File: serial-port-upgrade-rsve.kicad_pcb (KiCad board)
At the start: 4 copper layers, 35.6 x 43.2 mm, 14 parts, among them J1 MFP RC, J2 MFP TDO, J3 VCC, J4 GND, J5 Led, J6 IDC connector, U1 GAL16V8_PHY, U2 12-STAGE_BINARY_RIPPLE_COUNTE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, X1 1,8432 MHz

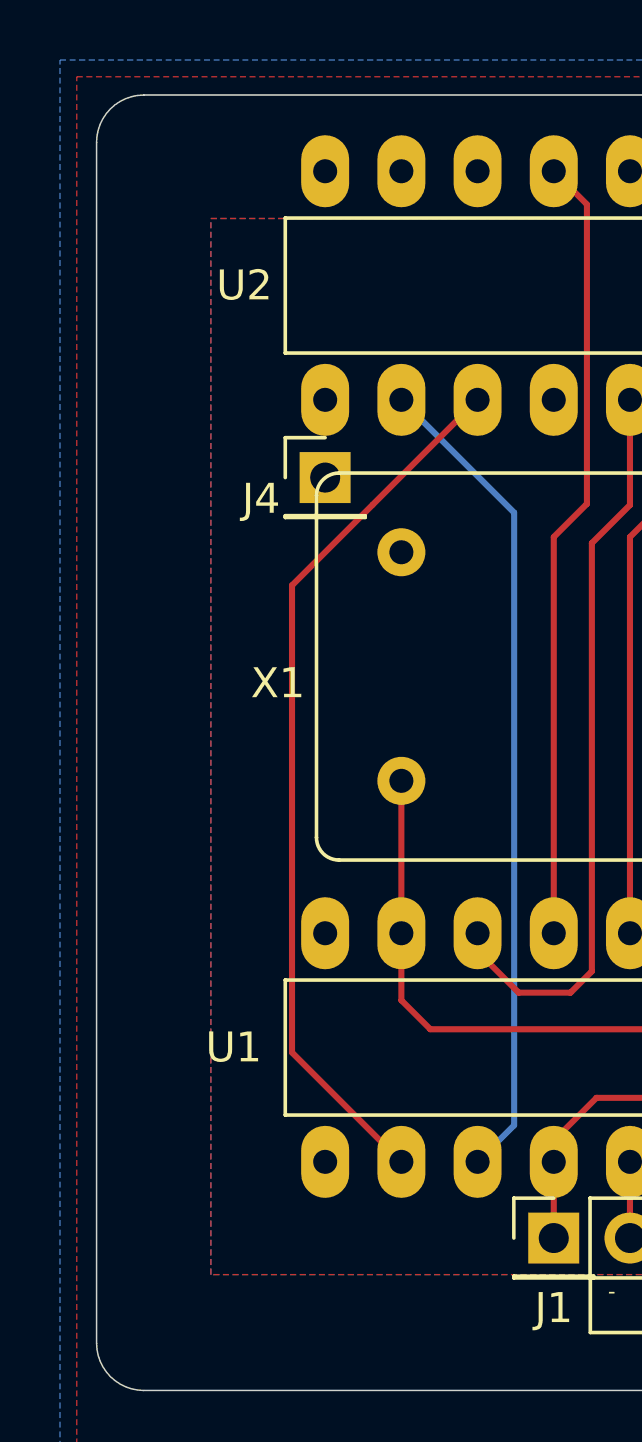
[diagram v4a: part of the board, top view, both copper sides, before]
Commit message: licence logo, title and disclaimer on PCB
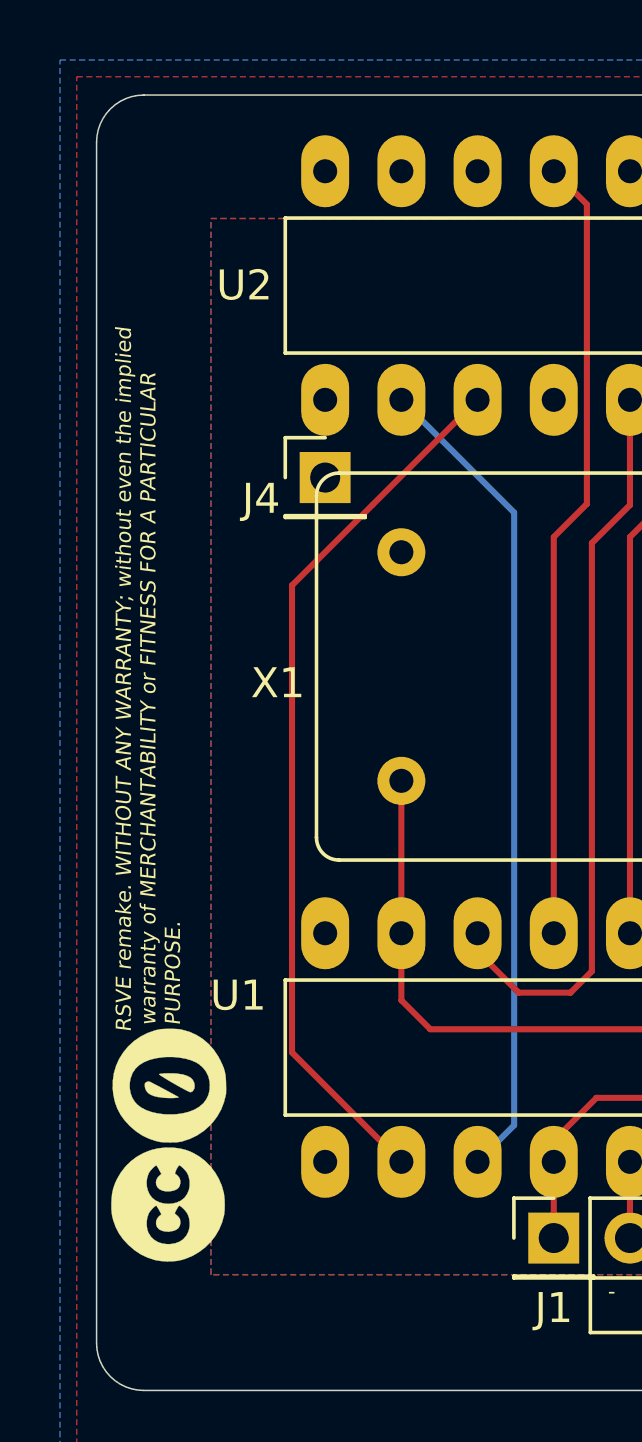
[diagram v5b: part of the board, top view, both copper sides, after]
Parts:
- added G***: LOGO, cliparts:logo--cc--zero, F.Cu at (78.6, 109.2)
- added G***: LOGO, cliparts:logo--cc--cc, F.Cu at (78.6, 113.1)
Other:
- board text added: "RSVE remake. WITHOUT ANY WARRANTY; without even the implied warranty of MERCHANTABILITY or FITNESS FOR A PARTICULAR PURPOSE."

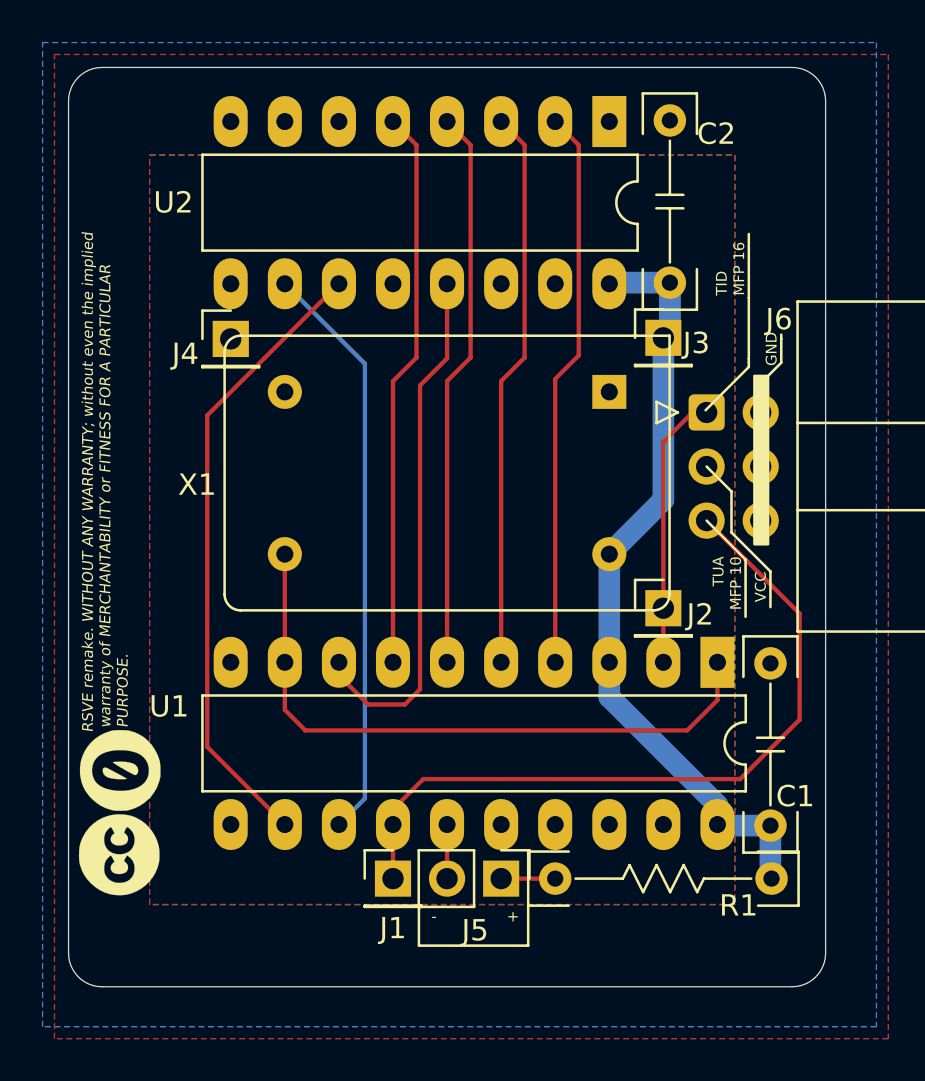
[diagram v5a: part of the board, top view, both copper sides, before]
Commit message: added mounting hole
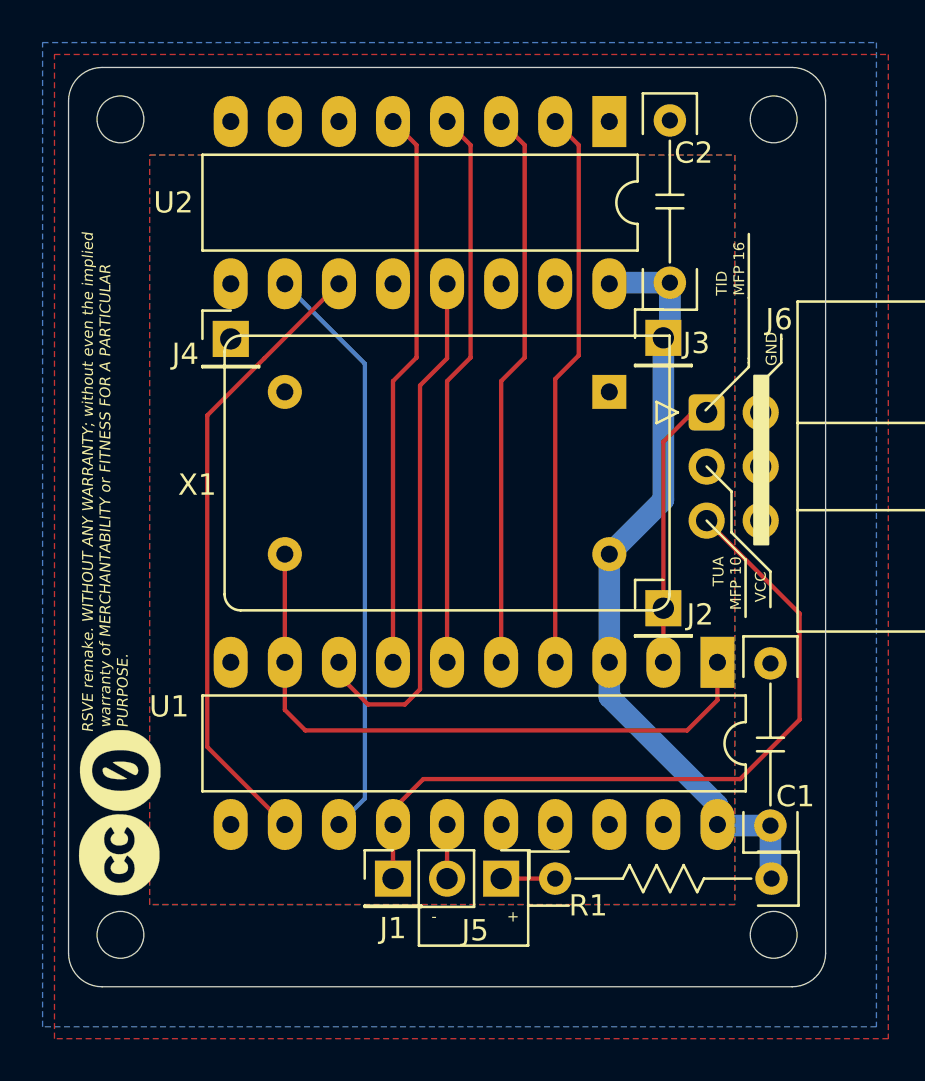
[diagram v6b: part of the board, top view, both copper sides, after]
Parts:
- added H1: M2, MountingHole:MountingHole_2.2mm_M2, F.Cu at (78.6, 78.6)
- added H2: M2, MountingHole:MountingHole_2.2mm_M2, F.Cu at (109.3, 78.6)
- added H3: M2, MountingHole:MountingHole_2.2mm_M2, F.Cu at (109.3, 116.9)
- added H4: M2, MountingHole:MountingHole_2.2mm_M2, F.Cu at (78.6, 116.9)
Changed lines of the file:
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@@
     (tracks 63)
     (zones 0)
-    (modules 16)
+    (modules 20)
     (nets 27)
   )
@@
     (add_net GND)
     (add_net VCC)
+  )
+  (module MountingHole:MountingHole_2.2mm_M2 (layer F.Cu)
+    (at 78.6384 116.8908)
+    (descr "Mounting Hole 2.2mm, no annular, M2")
+    (tags "mounting hole 2.2mm no annular m2")
+    (attr virtual)
+    (fp_text reference H4 (at 0 -3.2) (layer F.Fab)
+      (effects (font (size 1 1) (thickness 0.15)))
+    )
+    (fp_text value M2 (at 0 3.2) (layer F.Fab)
+      (effects (font (size 1 1) (thickness 0.15)))
+    )
+    (fp_text user %R (at 0.3 0) (layer F.Fab)
+      (effects (font (size 1 1) (thickness 0.15)))
+    )
+    (fp_circle (center 0 0) (end 2.2 0) (layer Cmts.User) (width 0.15))
+    (fp_circle (center 0 0) (end 2.45 0) (layer F.CrtYd) (width 0.05))
+    (pad 1 np_thru_hole circle (at 0 0) (size 2.2 2.2) (drill 2.2) (layers *.Cu *.Mask))
+  )
+  (module MountingHole:MountingHole_2.2mm_M2 (layer F.Cu)
+    (at 109.3216 116.8908)
+    (descr "Mounting Hole 2.2mm, no annular, M2")
+    (tags "mounting hole 2.2mm no annular m2")
+    (attr virtual)
+    (fp_text reference H3 (at 0 -3.2) (layer F.Fab)
+      (effects (font (size 1 1) (thickness 0.15)))
+    )
+    (fp_text value M2 (at 0 3.2) (layer F.Fab)
+      (effects (font (size 1 1) (thickness 0.15)))
+    )
+    (fp_text user %R (at 0.3 0) (layer F.Fab)
+      (effects (font (size 1 1) (thickness 0.15)))
+    )
+    (fp_circle (center 0 0) (end 2.2 0) (layer Cmts.User) (width 0.15))
+    (fp_circle (center 0 0) (end 2.45 0) (layer F.CrtYd) (width 0.05))
+    (pad 1 np_thru_hole circle (at 0 0) (size 2.2 2.2) (drill 2.2) (layers *.Cu *.Mask))
+  )
+  (module MountingHole:MountingHole_2.2mm_M2 (layer F.Cu)
+    (at 109.3216 78.5876)
+    (descr "Mounting Hole 2.2mm, no annular, M2")
+    (tags "mounting hole 2.2mm no annular m2")
+    (attr virtual)
+    (fp_text reference H2 (at 0 -3.2) (layer F.Fab)
+      (effects (font (size 1 1) (thickness 0.15)))
+    )
+    (fp_text value M2 (at 0 3.2) (layer F.Fab)
+      (effects (font (size 1 1) (thickness 0.15)))
+    )
+    (fp_text user %R (at 0.3 0) (layer F.Fab)
+      (effects (font (size 1 1) (thickness 0.15)))
+    )
+    (fp_circle (center 0 0) (end 2.2 0) (layer Cmts.User) (width 0.15))
+    (fp_circle (center 0 0) (end 2.45 0) (layer F.CrtYd) (width 0.05))
+    (pad 1 np_thru_hole circle (at 0 0) (size 2.2 2.2) (drill 2.2) (layers *.Cu *.Mask))
+  )
+  (module MountingHole:MountingHole_2.2mm_M2 (layer F.Cu)
+    (at 78.6384 78.5876)
+    (descr "Mounting Hole 2.2mm, no annular, M2")
+    (tags "mounting hole 2.2mm no annular m2")
+    (attr virtual)
+    (fp_text reference H1 (at 0 -3.2) (layer F.Fab)
+      (effects (font (size 1 1) (thickness 0.15)))
+    )
+    (fp_text value M2 (at 0 3.2) (layer F.Fab)
+      (effects (font (size 1 1) (thickness 0.15)))
+    )
+    (fp_text user %R (at 0.3 0) (layer F.Fab)
+      (effects (font (size 1 1) (thickness 0.15)))
+    )
+    (fp_circle (center 0 0) (end 2.2 0) (layer Cmts.User) (width 0.15))
+    (fp_circle (center 0 0) (end 2.45 0) (layer F.CrtYd) (width 0.05))
+    (pad 1 np_thru_hole circle (at 0 0) (size 2.2 2.2) (drill 2.2) (layers *.Cu *.Mask))
   )
   (module cliparts:logo--cc--zero (layer F.Cu)
@@
     (descr "THT resistor, width 100mils, lead vias 400mils apart")
     (tags "axial resistor tht")
-    (fp_text reference R1 (at -4.445 -1.27) (layer F.SilkS)
-      (effects (font (size 1 1) (thickness 0.15)) (justify right))
+    (fp_text reference R1 (at 4.445 -1.27) (layer F.SilkS)
+      (effects (font (size 1 1) (thickness 0.15)) (justify left))
     )
     (fp_text value 1K (at 0 -0.5) (layer F.Fab)
@@
     (descr "MLCC THT axial capacitor, width 100mils, lead vias 300mils apart")
     (tags "mlcc axial capacitor tht")
-    (fp_text reference C2 (at 3.175 1.27 180) (layer F.SilkS)
+    (fp_text reference C2 (at 2.286 0.2032 180) (layer F.SilkS)
       (effects (font (size 1 1) (thickness 0.15)) (justify left))
     )

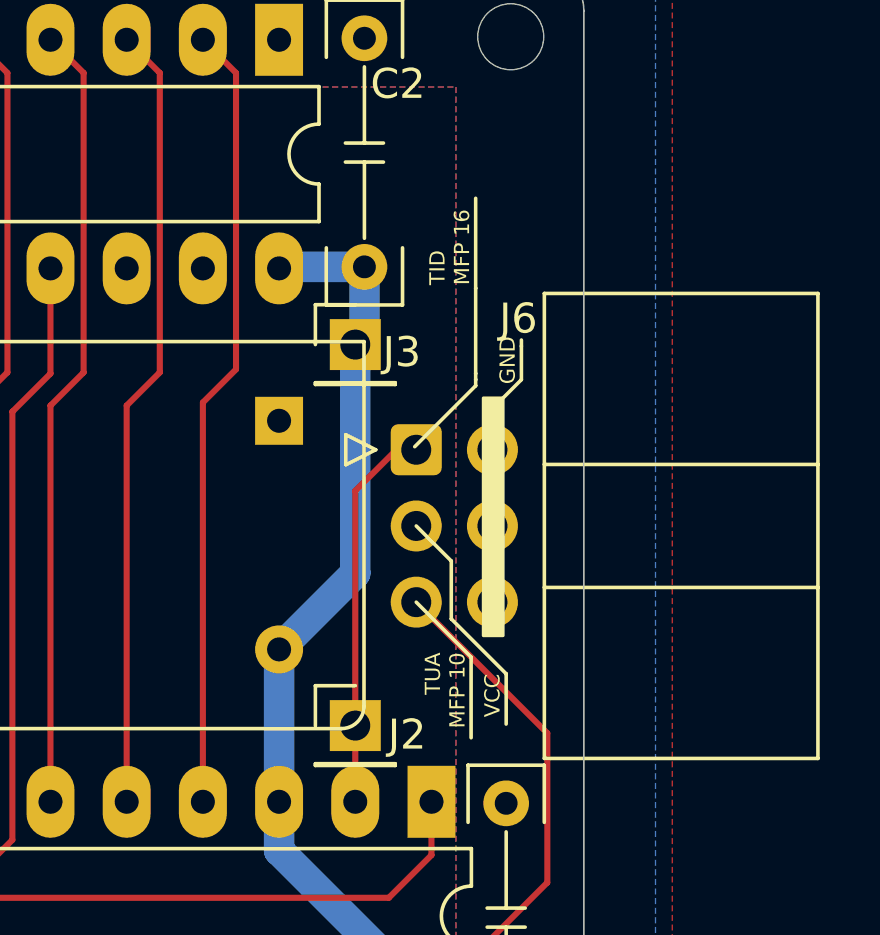
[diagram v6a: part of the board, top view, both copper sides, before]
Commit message: silkscreen : replace MFP pin number mentions (DIP 48 specific) by pin names
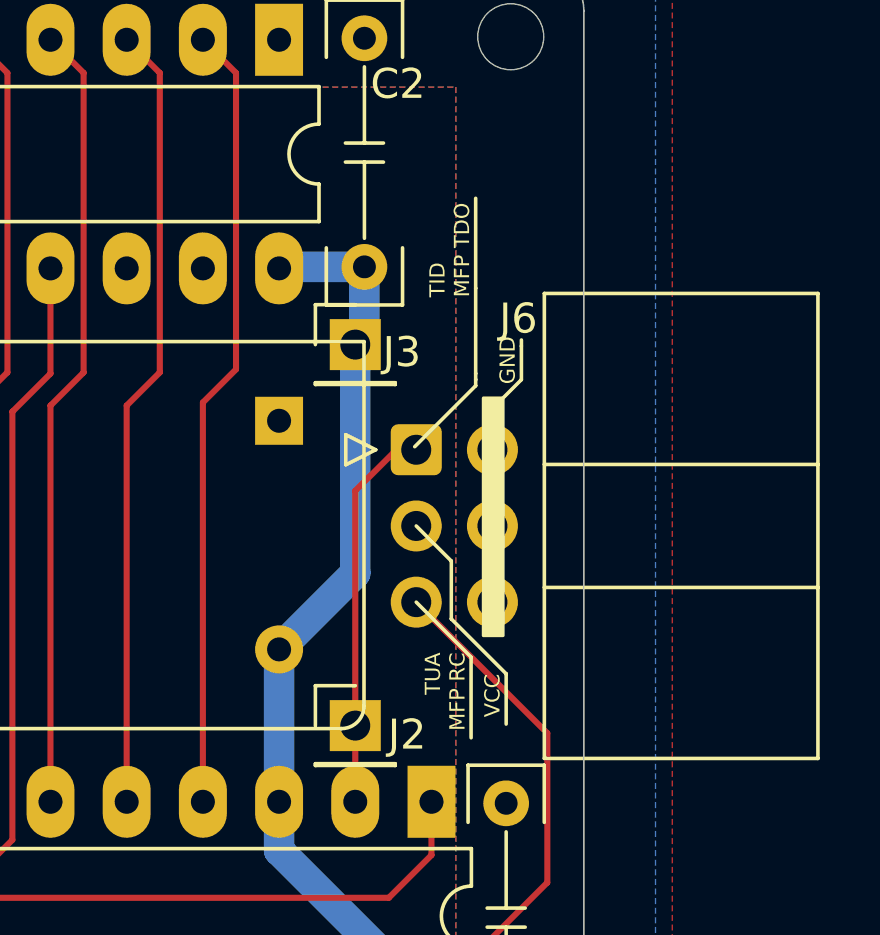
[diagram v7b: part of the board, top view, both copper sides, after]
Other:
- board text added: "TID MFP TDO"
- board text added: "TUA MFP RC"
- board text removed: "TID MFP 16"
- board text removed: "TUA MFP 10"

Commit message: last tweaks on the silkscreen : repository url, notice/disclaimer on the front
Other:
- board text added: "https://github.com/sporniket/atari-st-mod-serial-port-upgrade-rsve"
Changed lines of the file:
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@@
   (general
     (thickness 1.6)
-    (drawings 34)
+    (drawings 35)
     (tracks 63)
     (zones 0)
@@
       (net 2 VCC))
   )
+  (gr_text https://github.com/sporniket/atari-st-mod-serial-port-upgrade-rsve (at 81.534 97.6884 90) (layer B.SilkS)
+    (effects (font (size 0.762 0.762) (thickness 0.1016)) (justify mirror))
+  )
   (gr_text "RSVE remake. WITHOUT ANY WARRANTY; without even the implied\n warranty of MERCHANTABILITY or FITNESS FOR A PARTICULAR\n PURPOSE." (at 77.9272 107.3912 90) (layer F.SilkS)
